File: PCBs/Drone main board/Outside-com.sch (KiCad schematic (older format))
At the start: 25 parts, among them J901 Amphenol-1mm-10-header

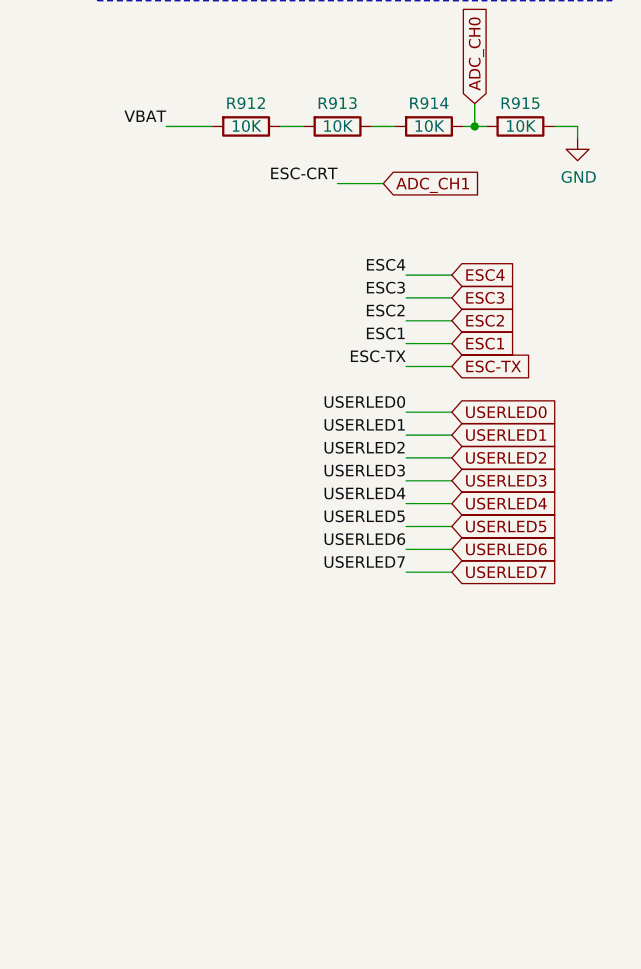
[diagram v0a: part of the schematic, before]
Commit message: Some cleanup, and PCB antenna removal.
Last edits before asking for reddit feedback.

Signed-off-by: Eldalote.Electronics <Eldalote.Electronics@gmail.com>
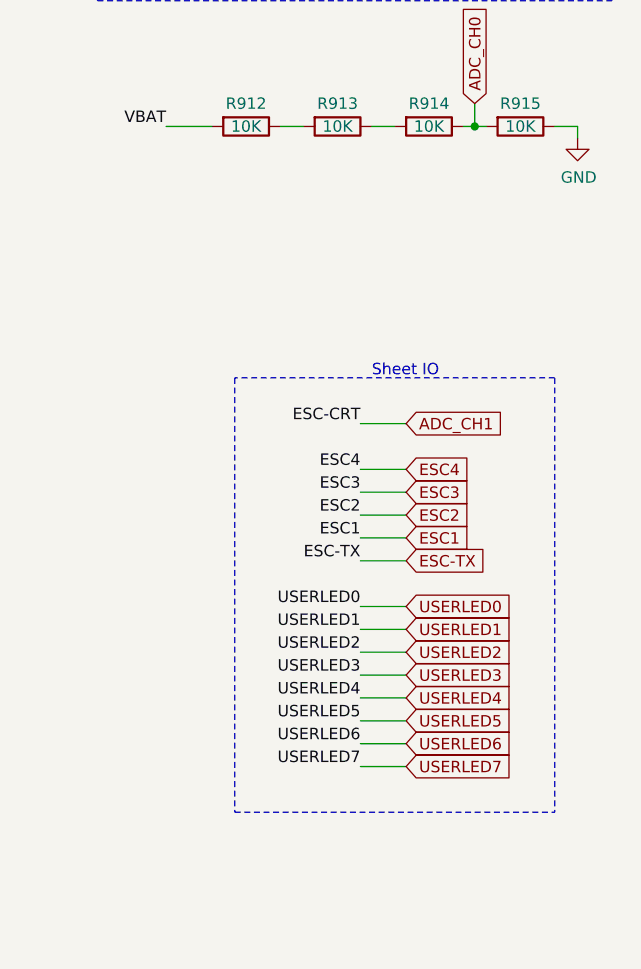
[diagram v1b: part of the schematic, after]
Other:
- note added: "Sheet IO"
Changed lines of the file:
@@
 USERLED7
 Wire Wire Line
-	10350 3500 10150 3500
+	10150 4350 9950 4350
 Wire Wire Line
-	10350 3600 10150 3600
+	10150 4450 9950 4450
 Wire Wire Line
-	10350 3700 10150 3700
+	10150 4550 9950 4550
 Wire Wire Line
-	10350 3800 10150 3800
-Text Label 10150 3500 2    50   ~ 0
+	10150 4650 9950 4650
+Text Label 9950 4350 2    50   ~ 0
 ESC4
-Text Label 10150 3600 2    50   ~ 0
+Text Label 9950 4450 2    50   ~ 0
 ESC3
-Text Label 10150 3700 2    50   ~ 0
+Text Label 9950 4550 2    50   ~ 0
 ESC2
-Text Label 10150 3800 2    50   ~ 0
+Text Label 9950 4650 2    50   ~ 0
 ESC1
-Text Label 9850 3100 2    50   ~ 0
+Text Label 9950 4150 2    50   ~ 0
 ESC-CRT
-Text Label 10150 3900 2    50   ~ 0
+Text Label 9950 4750 2    50   ~ 0
 ESC-TX
 Wire Wire Line
-	10050 3100 9850 3100
+	10150 4150 9950 4150
 Wire Wire Line
-	10350 3900 10150 3900
+	10150 4750 9950 4750
 Wire Wire Line
-	10150 4100 10350 4100
+	9950 4950 10150 4950
 Wire Wire Line
-	10150 4200 10350 4200
+	9950 5050 10150 5050
 Wire Wire Line
-	10150 4300 10350 4300
+	9950 5150 10150 5150
 Wire Wire Line
-	10150 4400 10350 4400
+	9950 5250 10150 5250
 Wire Wire Line
-	10150 4500 10350 4500
+	9950 5350 10150 5350
 Wire Wire Line
-	10150 4600 10350 4600
+	9950 5450 10150 5450
 Wire Wire Line
-	10150 4700 10350 4700
+	9950 5550 10150 5550
 Wire Wire Line
-	10150 4800 10350 4800
-Text Label 10150 4100 2    50   ~ 0
+	9950 5650 10150 5650
+Text Label 9950 4950 2    50   ~ 0
 USERLED0
-Text Label 10150 4200 2    50   ~ 0
+Text Label 9950 5050 2    50   ~ 0
 USERLED1
-Text Label 10150 4300 2    50   ~ 0
+Text Label 9950 5150 2    50   ~ 0
 USERLED2
-Text Label 10150 4400 2    50   ~ 0
+Text Label 9950 5250 2    50   ~ 0
 USERLED3
-Text Label 10150 4500 2    50   ~ 0
+Text Label 9950 5350 2    50   ~ 0
 USERLED4
-Text Label 10150 4600 2    50   ~ 0
+Text Label 9950 5450 2    50   ~ 0
 USERLED5
-Text Label 10150 4700 2    50   ~ 0
+Text Label 9950 5550 2    50   ~ 0
 USERLED6
-Text Label 10150 4800 2    50   ~ 0
+Text Label 9950 5650 2    50   ~ 0
 USERLED7
-Text GLabel 10350 3500 2    50   Input ~ 0
+Text GLabel 10150 4350 2    50   Input ~ 0
 ESC4
-Text GLabel 10350 3600 2    50   Input ~ 0
+Text GLabel 10150 4450 2    50   Input ~ 0
 ESC3
-Text GLabel 10350 3700 2    50   Input ~ 0
+Text GLabel 10150 4550 2    50   Input ~ 0
 ESC2
-Text GLabel 10350 3800 2    50   Input ~ 0
+Text GLabel 10150 4650 2    50   Input ~ 0
 ESC1
-Text GLabel 10350 3900 2    50   Input ~ 0
+Text GLabel 10150 4750 2    50   Input ~ 0
 ESC-TX
 $Comp
@@
 Wire Wire Line
 	10450 2850 10400 2850
-Text GLabel 10350 4100 2    50   Input ~ 0
+Text GLabel 10150 4950 2    50   Input ~ 0
 USERLED0
-Text GLabel 10350 4200 2    50   Input ~ 0
+Text GLabel 10150 5050 2    50   Input ~ 0
 USERLED1
-Text GLabel 10350 4300 2    50   Input ~ 0
+Text GLabel 10150 5150 2    50   Input ~ 0
 USERLED2
-Text GLabel 10350 4400 2    50   Input ~ 0
+Text GLabel 10150 5250 2    50   Input ~ 0
 USERLED3
-Text GLabel 10350 4500 2    50   Input ~ 0
+Text GLabel 10150 5350 2    50   Input ~ 0
 USERLED4
-Text GLabel 10350 4600 2    50   Input ~ 0
+Text GLabel 10150 5450 2    50   Input ~ 0
 USERLED5
-Text GLabel 10350 4700 2    50   Input ~ 0
+Text GLabel 10150 5550 2    50   Input ~ 0
 USERLED6
-Text GLabel 10350 4800 2    50   Input ~ 0
+Text GLabel 10150 5650 2    50   Input ~ 0
 USERLED7
-Text GLabel 10050 3100 2    50   Input ~ 0
+Text GLabel 10150 4150 2    50   Input ~ 0
 ADC_CH1
 $Comp
@@
 $EndComp
 Connection ~ 9300 1500
+Wire Notes Line
+	10800 3950 9400 3950
+Wire Notes Line
+	9400 3950 9400 5850
+Wire Notes Line
+	9400 5850 10800 5850
+Wire Notes Line
+	10800 3950 10800 5850
+Text Notes 10000 3950 0    50   ~ 0
+Sheet IO
 $EndSCHEMATC

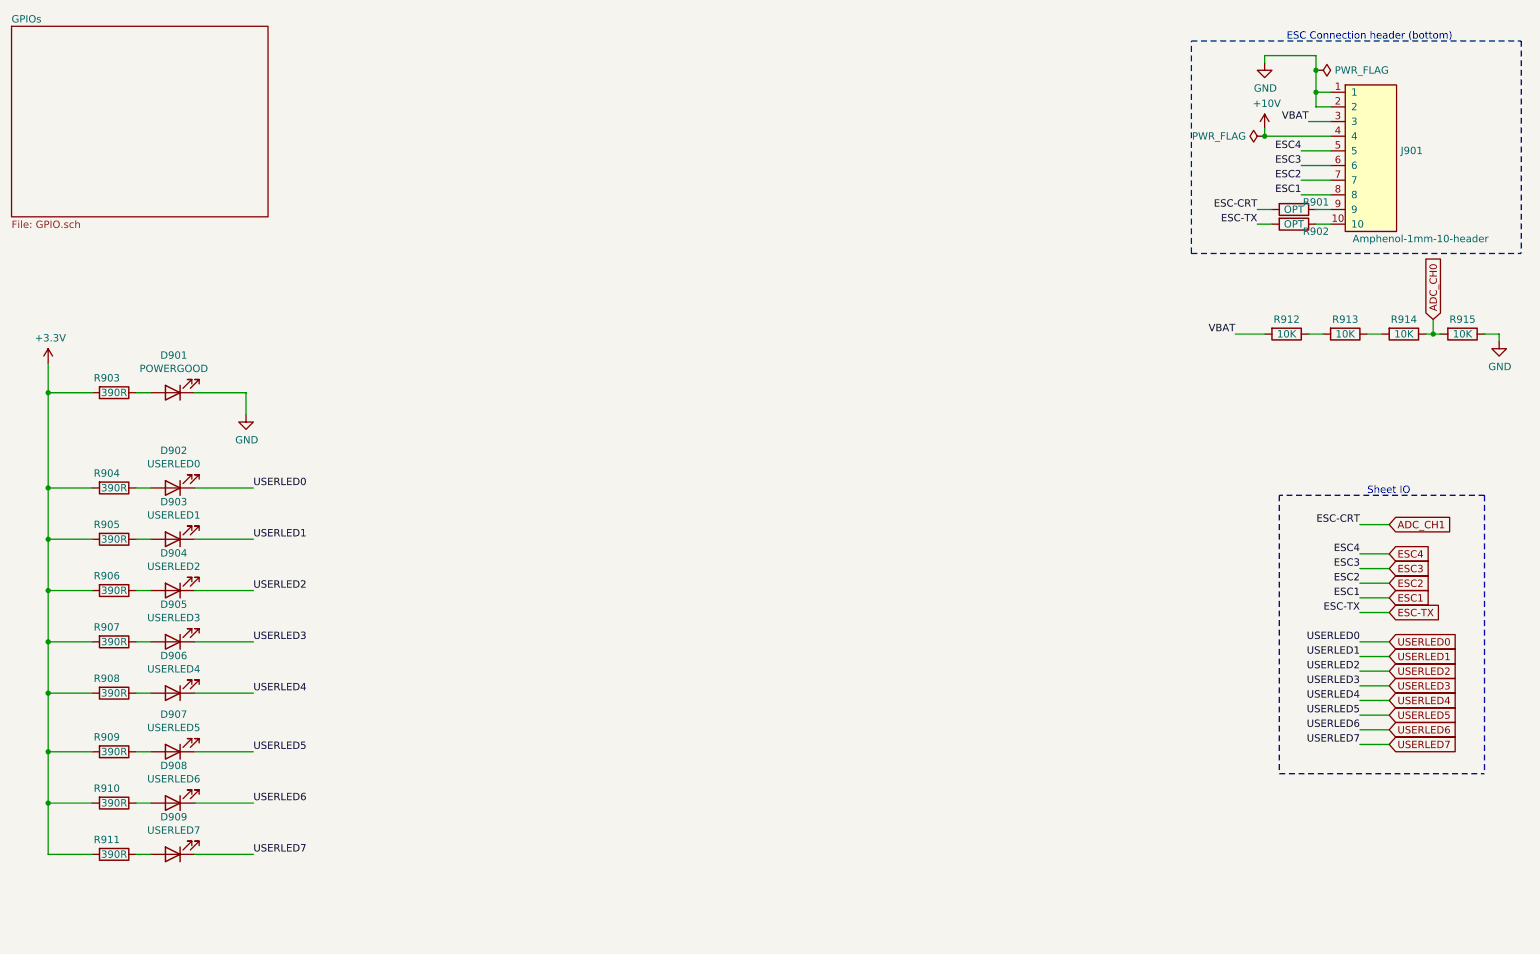
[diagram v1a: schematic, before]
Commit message: Finished (?) the schematic check and update. Next: PCB update
Signed-off-by: Eldalote.Electronics <Eldalote.Electronics@gmail.com>
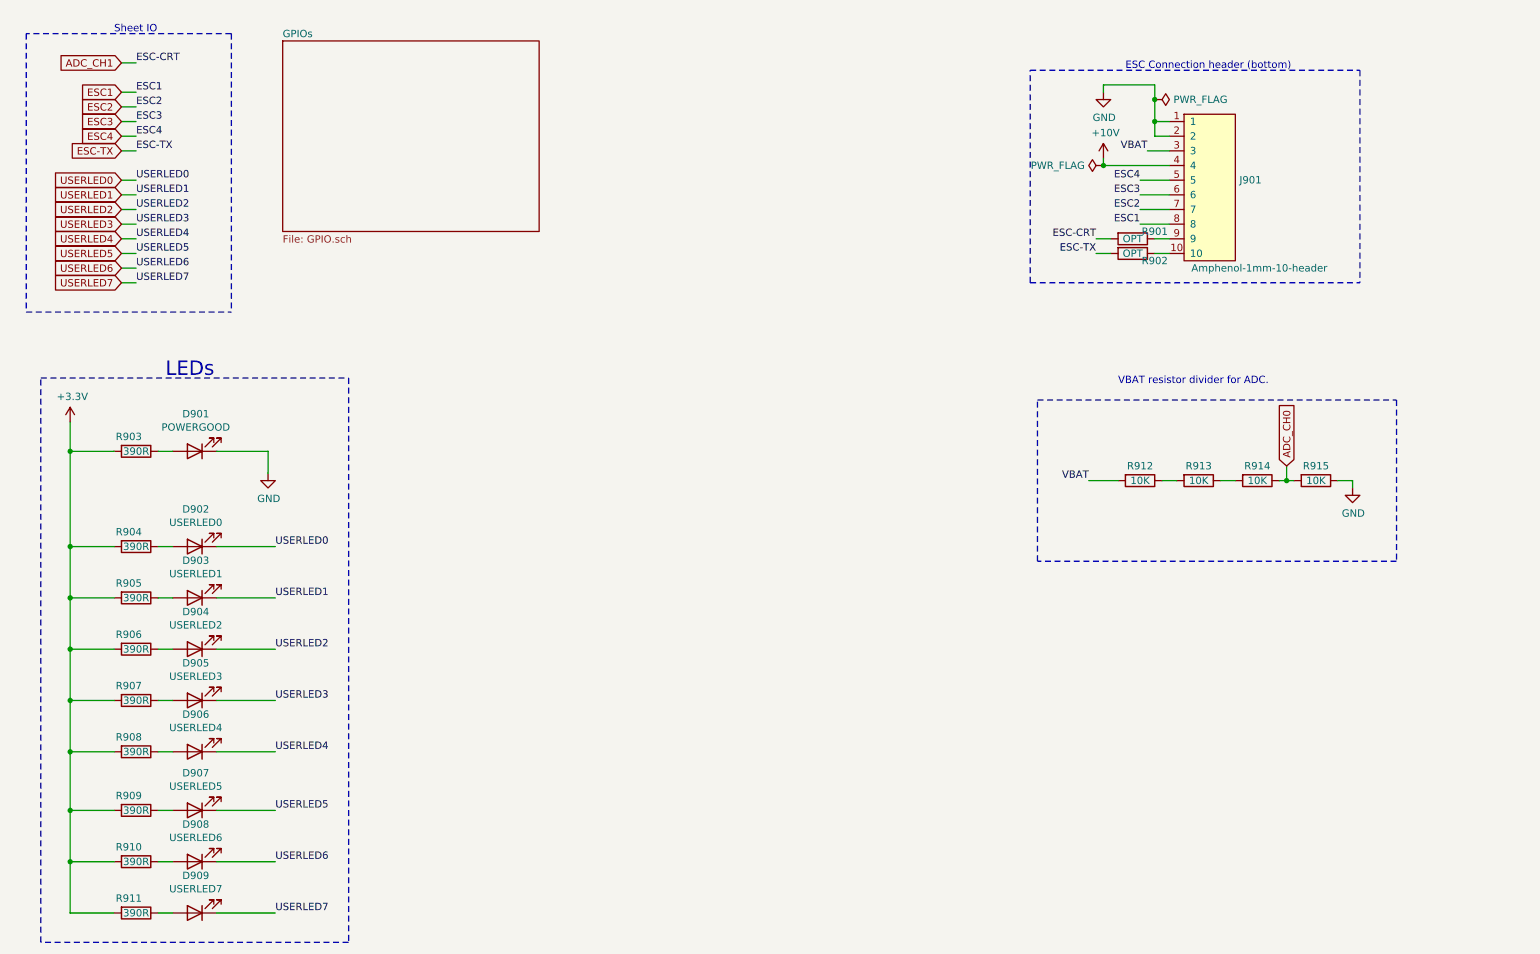
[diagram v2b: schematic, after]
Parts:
- D901, D902, D903, D904, D905, D906, D907, D908, D909: LCSC C72041 -> (none); MfNr (none) -> SML-D12M8WT86
- J901: DigiKey 609-6308-1-ND -> (none); MfNr (none) -> 10147606-00010LF; Mouser 649-10147606-00010LF -> (none)
- R903, R904, R905, R906, R907, R908, R909, R910, R911: footprint Resistor_SMD:R_0603_1608Metric -> Resistor_SMD:R_0402_1005Metric; LCSC C23151 -> (none); MfNr (none) -> RMCF0402FT390R
- R912, R913, R914, R915: footprint Resistor_SMD:R_0805_2012Metric -> Resistor_SMD:R_0402_1005Metric; LCSC C17414 -> (none); MfNr (none) -> RC0402FR-0710KL
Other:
- note added: "LEDs"
- note added: "VBAT resistor divider for ADC."
- moved on the sheet: D901, D902, D903, D904, D905, D906, D907, D908, D909, J901, R901, R902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
